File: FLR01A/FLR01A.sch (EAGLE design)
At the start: 10 parts, among them J1 M10SMD_MALE, J2 M10SMD_MALE

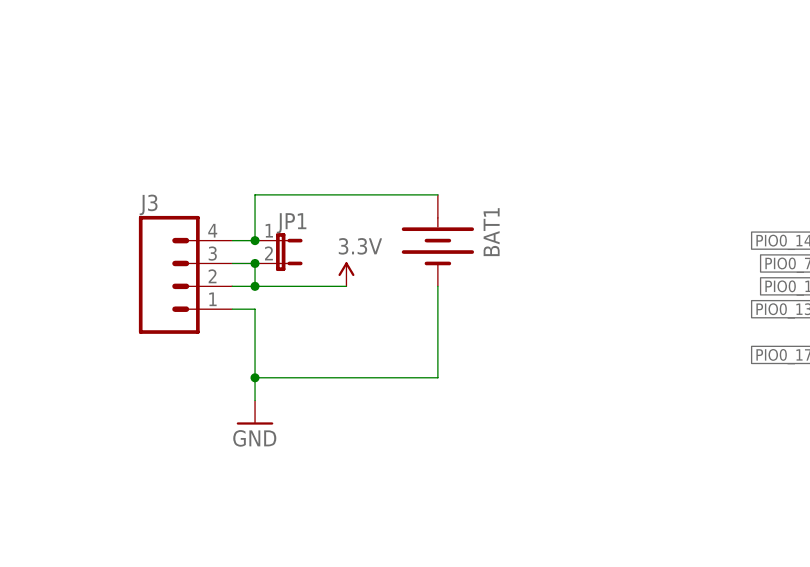
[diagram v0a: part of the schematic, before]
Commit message: [flr] add ptc fuse in series with battery
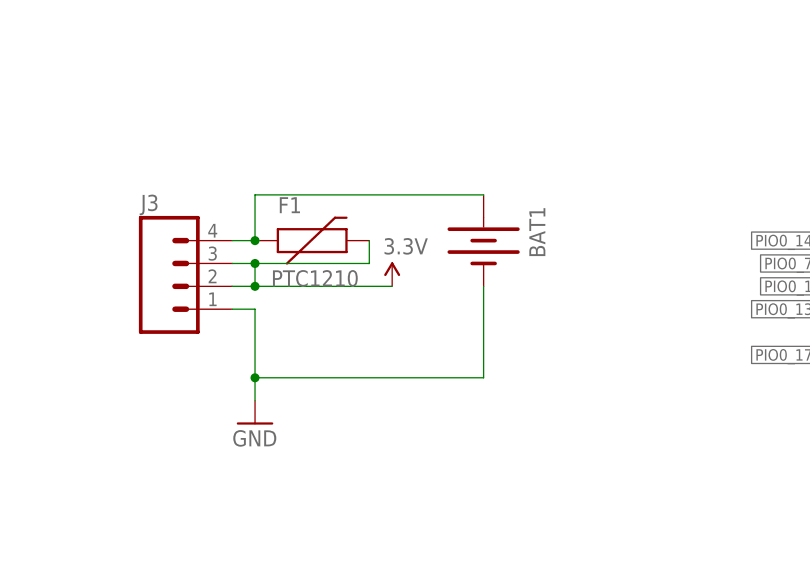
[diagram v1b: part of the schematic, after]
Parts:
- removed JP1: (no value), SparkFun-Passives:JUMPER-2SMD-NC
- added F1: PTC1210, flukso:PTC1210
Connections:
- net 3.3V: now also F1.2; no longer JP1.2
- net N$1: now also F1.1; no longer JP1.1
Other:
- moved on the sheet: BAT1
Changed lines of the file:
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@@
 <part name="BAT1" library="SparkFun-Electromechanical" deviceset="BATTERY" device="245PTH"/>
 <part name="GND1" library="sparkFun" deviceset="GND" device=""/>
-<part name="JP1" library="SparkFun-Passives" deviceset="JUMPER-2" device="SMD-NC"/>
 <part name="P+1" library="sparkFun" deviceset="3.3V" device=""/>
 <part name="J3" library="SparkFun-Connectors" deviceset="M04" device="1X04_NO_SILK"/>
@@
 <part name="S1" library="SparkFun-Electromechanical" deviceset="SWITCH-MOMENTARY-2" device="SMD"/>
 <part name="GND2" library="sparkFun" deviceset="GND" device=""/>
+<part name="F1" library="flukso" deviceset="PTC" device="1210"/>
 </parts>
 <sheets>
@@
 <instance part="FRAME1" gate="G$2" x="162.56" y="0"/>
 <instance part="U$1" gate="G$1" x="15.24" y="12.7"/>
-<instance part="P+2" gate="G$1" x="99.06" y="96.52"/>
+<instance part="P+2" gate="G$1" x="104.14" y="96.52"/>
 <instance part="GND8" gate="1" x="165.1" y="78.74"/>
 <instance part="C1" gate="G$1" x="187.96" y="104.14"/>
@@
 <attribute name="NAME" x="55.88" y="171.45" size="1.778" layer="95"/>
 </instance>
-<instance part="BAT1" gate="G$1" x="109.22" y="101.6" rot="R270"/>
+<instance part="BAT1" gate="G$1" x="114.3" y="101.6" rot="R270"/>
 <instance part="GND1" gate="1" x="88.9" y="81.28"/>
-<instance part="JP1" gate="A" x="91.44" y="101.6" rot="R270"/>
 <instance part="P+1" gate="G$1" x="167.64" y="111.76"/>
 <instance part="J3" gate="G$1" x="81.28" y="96.52"/>
@@
 </instance>
 <instance part="GND2" gate="1" x="40.64" y="139.7"/>
+<instance part="F1" gate="G$1" x="93.98" y="101.6"/>
 </instances>
 <busses>
@@
 <pinref part="BAT1" gate="G$1" pin="-"/>
 <wire x1="88.9" y1="86.36" x2="88.9" y2="83.82" width="0.1524" layer="91"/>
-<wire x1="109.22" y1="96.52" x2="109.22" y2="86.36" width="0.1524" layer="91"/>
-<wire x1="109.22" y1="86.36" x2="88.9" y2="86.36" width="0.1524" layer="91"/>
+<wire x1="114.3" y1="96.52" x2="114.3" y2="86.36" width="0.1524" layer="91"/>
+<wire x1="114.3" y1="86.36" x2="88.9" y2="86.36" width="0.1524" layer="91"/>
 <junction x="88.9" y="86.36"/>
 <pinref part="J3" gate="G$1" pin="1"/>
@@
 </segment>
 <segment>
-<pinref part="JP1" gate="A" pin="2"/>
 <pinref part="J3" gate="G$1" pin="3"/>
 <wire x1="88.9" y1="99.06" x2="86.36" y2="99.06" width="0.1524" layer="91"/>
@@
 <wire x1="88.9" y1="99.06" x2="88.9" y2="96.52" width="0.1524" layer="91"/>
 <wire x1="88.9" y1="96.52" x2="86.36" y2="96.52" width="0.1524" layer="91"/>
+<pinref part="P+2" gate="G$1" pin="3.3V"/>
+<wire x1="88.9" y1="96.52" x2="104.14" y2="96.52" width="0.1524" layer="91"/>
+<junction x="88.9" y="96.52"/>
+<pinref part="F1" gate="G$1" pin="2"/>
+<wire x1="101.6" y1="101.6" x2="101.6" y2="99.06" width="0.1524" layer="91"/>
+<wire x1="101.6" y1="99.06" x2="88.9" y2="99.06" width="0.1524" layer="91"/>
 <junction x="88.9" y="99.06"/>
-<pinref part="P+2" gate="G$1" pin="3.3V"/>
-<wire x1="88.9" y1="96.52" x2="99.06" y2="96.52" width="0.1524" layer="91"/>
-<junction x="88.9" y="96.52"/>
 </segment>
 </net>
@@
 <segment>
 <pinref part="BAT1" gate="G$1" pin="+"/>
-<wire x1="109.22" y1="106.68" x2="88.9" y2="106.68" width="0.1524" layer="91"/>
+<wire x1="114.3" y1="106.68" x2="88.9" y2="106.68" width="0.1524" layer="91"/>
 <wire x1="88.9" y1="106.68" x2="88.9" y2="101.6" width="0.1524" layer="91"/>
 <pinref part="J3" gate="G$1" pin="4"/>
 <wire x1="88.9" y1="101.6" x2="86.36" y2="101.6" width="0.1524" layer="91"/>
-<pinref part="JP1" gate="A" pin="1"/>
+<pinref part="F1" gate="G$1" pin="1"/>
 <junction x="88.9" y="101.6"/>
 </segment>

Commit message: [flk/flr] introduce r3 of sensor and radio board
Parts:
- J1, J2: value M10SMD_MALE -> M10SMD_MALE_SHORT; device flukso:M10SMD_MALE -> flukso:M10SMD_MALE_SHORT
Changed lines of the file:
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@@
 <part name="U$5" library="flukso" deviceset="RFM12B" device=""/>
 <part name="GND25" library="sparkFun" deviceset="GND" device=""/>
-<part name="J1" library="flukso" deviceset="M10" device="SMD_MALE"/>
-<part name="J2" library="flukso" deviceset="M10" device="SMD_MALE"/>
 <part name="BAT1" library="SparkFun-Electromechanical" deviceset="BATTERY" device="245PTH"/>
 <part name="GND1" library="sparkFun" deviceset="GND" device=""/>
@@
 <part name="GND2" library="sparkFun" deviceset="GND" device=""/>
 <part name="F1" library="flukso" deviceset="PTC" device="1210"/>
+<part name="J1" library="flukso" deviceset="M10" device="SMD_MALE_SHORT"/>
+<part name="J2" library="flukso" deviceset="M10" device="SMD_MALE_SHORT"/>
 </parts>
 <sheets>
@@
 <instance part="U$5" gate="G$1" x="167.64" y="96.52"/>
 <instance part="GND25" gate="1" x="170.18" y="78.74"/>
-<instance part="J1" gate="G$1" x="10.16" y="162.56" smashed="yes">
-<attribute name="NAME" x="10.16" y="171.45" size="1.778" layer="95"/>
-</instance>
-<instance part="J2" gate="G$1" x="55.88" y="162.56" smashed="yes">
-<attribute name="NAME" x="55.88" y="171.45" size="1.778" layer="95"/>
-</instance>
 <instance part="BAT1" gate="G$1" x="114.3" y="101.6" rot="R270"/>
 <instance part="GND1" gate="1" x="88.9" y="81.28"/>
@@
 <instance part="GND2" gate="1" x="40.64" y="139.7"/>
 <instance part="F1" gate="G$1" x="93.98" y="101.6"/>
+<instance part="J1" gate="G$1" x="10.16" y="162.56" smashed="yes">
+<attribute name="NAME" x="10.16" y="171.45" size="1.778" layer="95"/>
+</instance>
+<instance part="J2" gate="G$1" x="55.88" y="162.56" smashed="yes">
+<attribute name="NAME" x="55.88" y="171.45" size="1.778" layer="95"/>
+</instance>
 </instances>
 <busses>
@@
 </segment>
 <segment>
-<pinref part="J2" gate="G$1" pin="6"/>
 <wire x1="66.04" y1="157.48" x2="68.58" y2="157.48" width="0.1524" layer="91"/>
 <label x="68.58" y="157.48" size="1.27" layer="95" xref="yes"/>
+<pinref part="J2" gate="G$1" pin="6"/>
 </segment>
 <segment>
@@
 <net name="3.3V" class="0">
 <segment>
-<pinref part="J2" gate="G$1" pin="5"/>
 <wire x1="66.04" y1="154.94" x2="68.58" y2="154.94" width="0.1524" layer="91"/>
 <label x="68.58" y="154.94" size="1.27" layer="95" xref="yes"/>
+<pinref part="J2" gate="G$1" pin="5"/>
 </segment>
 <segment>
@@
 <net name="PIO0_16" class="0">
 <segment>
-<pinref part="J1" gate="G$1" pin="10"/>
 <wire x1="20.32" y1="167.64" x2="22.86" y2="167.64" width="0.1524" layer="91"/>
 <label x="22.86" y="167.64" size="1.27" layer="95" xref="yes"/>
+<pinref part="J1" gate="G$1" pin="10"/>
 </segment>
 </net>
 <net name="I2C0_SCL" class="0">
 <segment>
-<pinref part="J1" gate="G$1" pin="9"/>
 <wire x1="20.32" y1="165.1" x2="22.86" y2="165.1" width="0.1524" layer="91"/>
 <label x="22.86" y="165.1" size="1.27" layer="95" xref="yes"/>
+<pinref part="J1" gate="G$1" pin="9"/>
 </segment>
 </net>
 <net name="I2C0_SDA" class="0">
 <segment>
-<pinref part="J1" gate="G$1" pin="8"/>
 <wire x1="20.32" y1="162.56" x2="22.86" y2="162.56" width="0.1524" layer="91"/>
 <label x="22.86" y="162.56" size="1.27" layer="95" xref="yes"/>
+<pinref part="J1" gate="G$1" pin="8"/>
 </segment>
 </net>
 <net name="PIO0_2" class="0">
 <segment>
-<pinref part="J1" gate="G$1" pin="7"/>
 <wire x1="20.32" y1="160.02" x2="22.86" y2="160.02" width="0.1524" layer="91"/>
 <label x="22.86" y="160.02" size="1.27" layer="95" xref="yes"/>
+<pinref part="J1" gate="G$1" pin="7"/>
 </segment>
 </net>
 <net name="PIO0_3" class="0">
 <segment>
-<pinref part="J1" gate="G$1" pin="6"/>
 <wire x1="20.32" y1="157.48" x2="22.86" y2="157.48" width="0.1524" layer="91"/>
 <label x="22.86" y="157.48" size="1.27" layer="95" xref="yes"/>
+<pinref part="J1" gate="G$1" pin="6"/>
 </segment>
 </net>
 <net name="PIO0_4" class="0">
 <segment>
-<pinref part="J1" gate="G$1" pin="5"/>
 <wire x1="20.32" y1="154.94" x2="22.86" y2="154.94" width="0.1524" layer="91"/>
 <label x="22.86" y="154.94" size="1.27" layer="95" xref="yes"/>
+<pinref part="J1" gate="G$1" pin="5"/>
 </segment>
 </net>
 <net name="PIO0_5" class="0">
 <segment>
-<pinref part="J1" gate="G$1" pin="4"/>
 <wire x1="20.32" y1="152.4" x2="40.64" y2="152.4" width="0.1524" layer="91"/>
 <label x="43.18" y="152.4" size="1.27" layer="95" xref="yes"/>
@@
 <wire x1="40.64" y1="152.4" x2="43.18" y2="152.4" width="0.1524" layer="91"/>
 <junction x="40.64" y="152.4"/>
+<pinref part="J1" gate="G$1" pin="4"/>
 </segment>
 </net>
 <net name="PIO0_12" class="0">
 <segment>
-<pinref part="J1" gate="G$1" pin="3"/>
 <wire x1="20.32" y1="149.86" x2="22.86" y2="149.86" width="0.1524" layer="91"/>
 <label x="22.86" y="149.86" size="1.27" layer="95" xref="yes"/>
+<pinref part="J1" gate="G$1" pin="3"/>
 </segment>
 </net>
 <net name="PIO0_13" class="0">
 <segment>
-<pinref part="J1" gate="G$1" pin="2"/>
 <wire x1="20.32" y1="147.32" x2="22.86" y2="147.32" width="0.1524" layer="91"/>
 <label x="22.86" y="147.32" size="1.27" layer="95" xref="yes"/>
+<pinref part="J1" gate="G$1" pin="2"/>
 </segment>
 <segment>
@@
 <net name="PIO0_17" class="0">
 <segment>
-<pinref part="J1" gate="G$1" pin="1"/>
 <wire x1="20.32" y1="144.78" x2="22.86" y2="144.78" width="0.1524" layer="91"/>
 <label x="22.86" y="144.78" size="1.27" layer="95" xref="yes"/>
+<pinref part="J1" gate="G$1" pin="1"/>
 </segment>
 <segment>
@@
 <net name="PIO0_14" class="0">
 <segment>
-<pinref part="J2" gate="G$1" pin="10"/>
 <wire x1="66.04" y1="167.64" x2="68.58" y2="167.64" width="0.1524" layer="91"/>
 <label x="68.58" y="167.64" size="1.27" layer="95" xref="yes"/>
+<pinref part="J2" gate="G$1" pin="10"/>
 </segment>
 <segment>
@@
 <net name="PIO0_0" class="0">
 <segment>
-<pinref part="J2" gate="G$1" pin="9"/>
 <wire x1="66.04" y1="165.1" x2="68.58" y2="165.1" width="0.1524" layer="91"/>
 <label x="68.58" y="165.1" size="1.27" layer="95" xref="yes"/>
+<pinref part="J2" gate="G$1" pin="9"/>
 </segment>
 </net>
 <net name="PIO0_6" class="0">
 <segment>
-<pinref part="J2" gate="G$1" pin="8"/>
 <wire x1="66.04" y1="162.56" x2="68.58" y2="162.56" width="0.1524" layer="91"/>
 <label x="68.58" y="162.56" size="1.27" layer="95" xref="yes"/>
+<pinref part="J2" gate="G$1" pin="8"/>
 </segment>
 </net>
 <net name="PIO0_7" class="0">
 <segment>
-<pinref part="J2" gate="G$1" pin="7"/>
 <wire x1="66.04" y1="160.02" x2="68.58" y2="160.02" width="0.1524" layer="91"/>
 <label x="68.58" y="160.02" size="1.27" layer="95" xref="yes"/>
+<pinref part="J2" gate="G$1" pin="7"/>
 </segment>
 <segment>
@@
 <net name="PIO0_8" class="0">
 <segment>
-<pinref part="J2" gate="G$1" pin="4"/>
 <wire x1="66.04" y1="152.4" x2="68.58" y2="152.4" width="0.1524" layer="91"/>
 <label x="68.58" y="152.4" size="1.27" layer="95" xref="yes"/>
+<pinref part="J2" gate="G$1" pin="4"/>
 </segment>
 </net>
 <net name="PIO0_9" class="0">
 <segment>
-<pinref part="J2" gate="G$1" pin="3"/>
 <wire x1="66.04" y1="149.86" x2="68.58" y2="149.86" width="0.1524" layer="91"/>
 <label x="68.58" y="149.86" size="1.27" layer="95" xref="yes"/>
+<pinref part="J2" gate="G$1" pin="3"/>
 </segment>
 </net>
 <net name="PIO0_1" class="0">
 <segment>
-<pinref part="J2" gate="G$1" pin="2"/>
 <wire x1="66.04" y1="147.32" x2="68.58" y2="147.32" width="0.1524" layer="91"/>
 <label x="68.58" y="147.32" size="1.27" layer="95" xref="yes"/>
+<pinref part="J2" gate="G$1" pin="2"/>
 </segment>
 <segment>
@@
 <net name="PIO0_15" class="0">
 <segment>
-<pinref part="J2" gate="G$1" pin="1"/>
 <wire x1="66.04" y1="144.78" x2="68.58" y2="144.78" width="0.1524" layer="91"/>
 <label x="68.58" y="144.78" size="1.27" layer="95" xref="yes"/>
-</segment>
-</net>
+<pinref part="J2" gate="G$1" pin="1"/>
+</segment>
+</net>

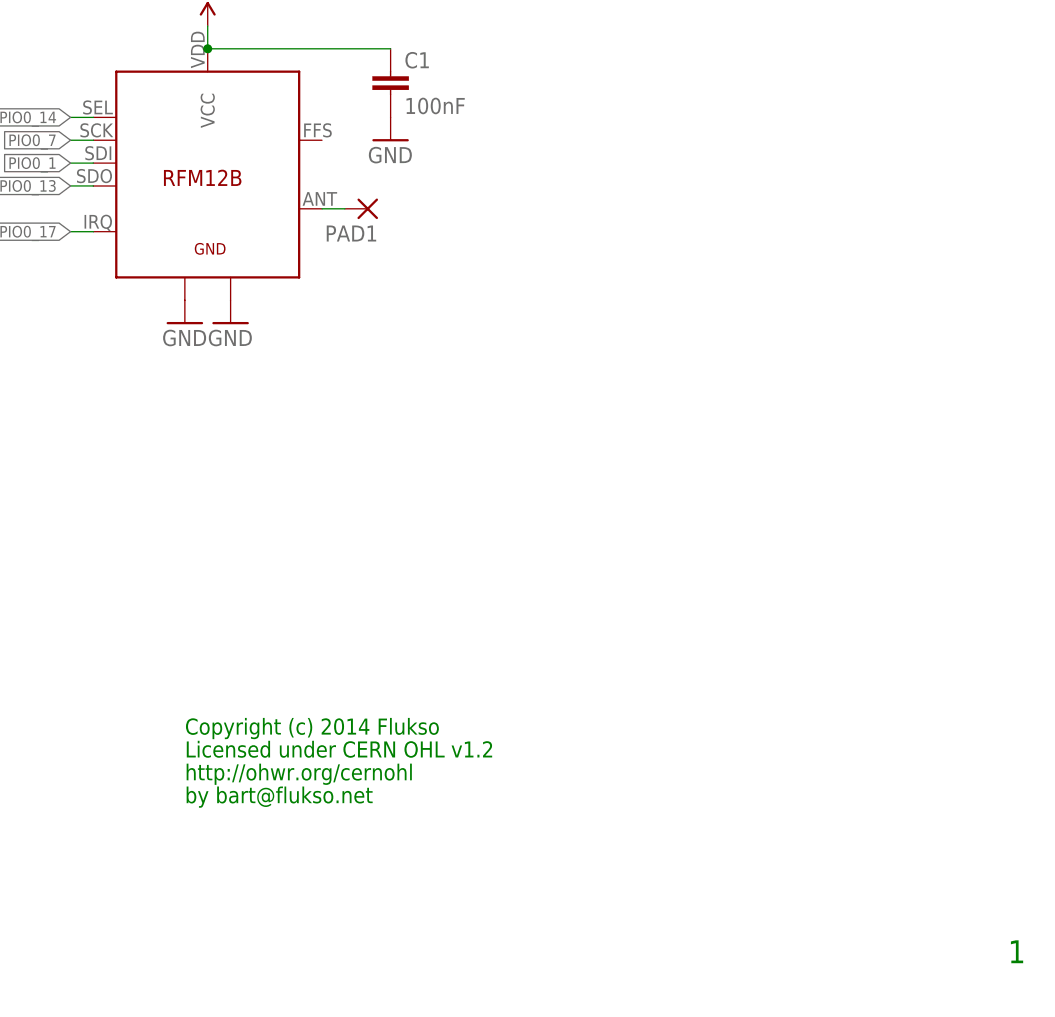
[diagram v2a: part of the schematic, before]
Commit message: [flk/flr] adapt board layout to new M10 footprints + power switch
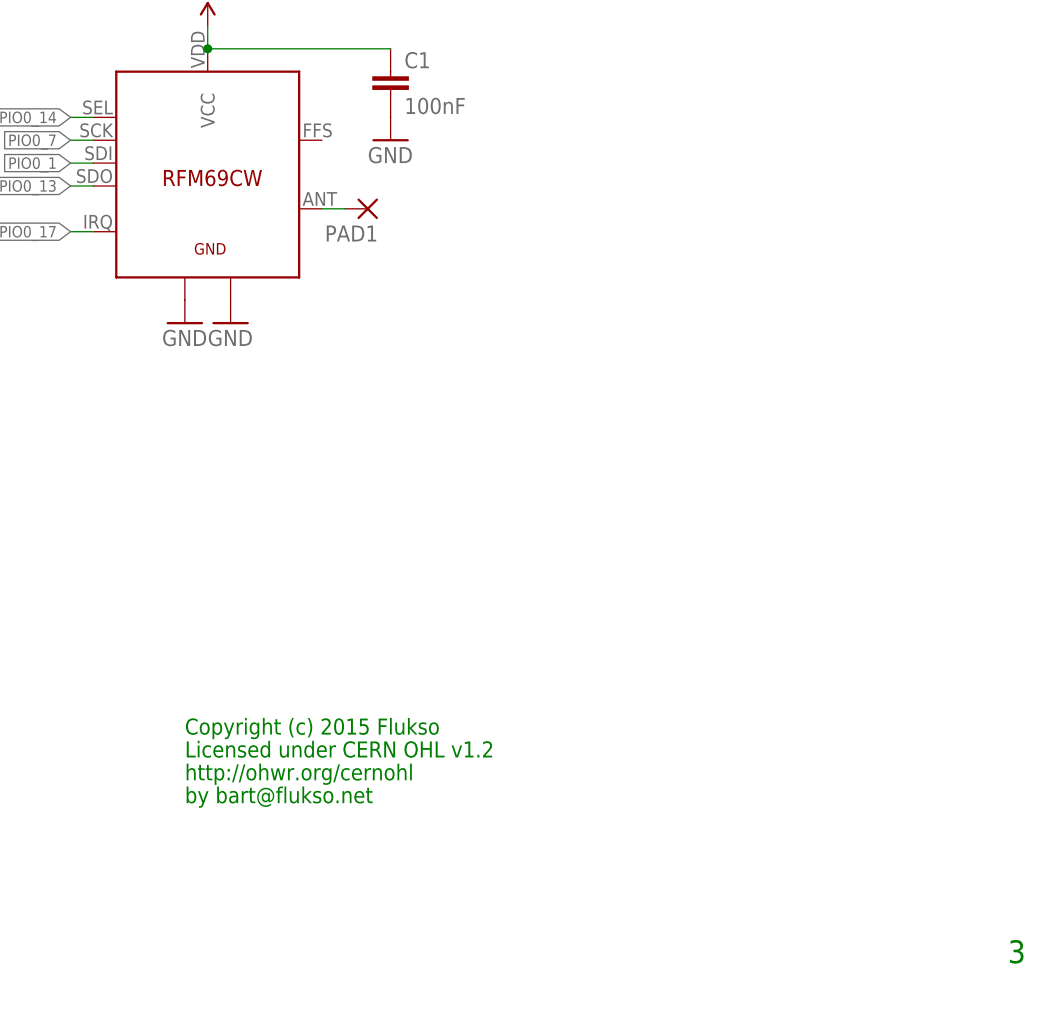
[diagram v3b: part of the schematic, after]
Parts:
- removed U$5: RFM12B, flukso:RFM12B
- added U$2: RFM69CW, flukso:RFM69CW
- J1, J2: value M10SMD_MALE_SHORT -> M10SMD_FEMALE_SHORT; device flukso:M10SMD_MALE_SHORT -> flukso:M10SMD_FEMALE_SHORT
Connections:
- net 3.3V: now also U$2.VCC; no longer U$5.VCC
- net GND: now also U$2.GND1, U$2.GND2; no longer U$5.GND1, U$5.GND2
- net N$6: now also U$2.ANT; no longer U$5.ANT
- net PIO0_1: now also U$2.SDI; no longer U$5.SDI
- net PIO0_13: now also U$2.SDO; no longer U$5.SDO
- net PIO0_14: now also U$2.SEL; no longer U$5.SEL
- net PIO0_17: now also U$2.IRQ; no longer U$5.IRQ
- net PIO0_7: now also U$2.SCK; no longer U$5.SCK
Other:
- note added: "3"
- note added: "Copyright (c) 2015 Flukso"
- note removed: "1"
- note removed: "Copyright (c) 2014 Flukso"
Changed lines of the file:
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@@
 <part name="C1" library="sparkFun" deviceset="CAP" device="0402-CAP" value="100nF"/>
 <part name="GND12" library="sparkFun" deviceset="GND" device=""/>
-<part name="U$5" library="flukso" deviceset="RFM12B" device=""/>
 <part name="GND25" library="sparkFun" deviceset="GND" device=""/>
 <part name="BAT1" library="SparkFun-Electromechanical" deviceset="BATTERY" device="245PTH"/>
@@
 <part name="GND2" library="sparkFun" deviceset="GND" device=""/>
 <part name="F1" library="flukso" deviceset="PTC" device="1210"/>
-<part name="J1" library="flukso" deviceset="M10" device="SMD_MALE_SHORT"/>
-<part name="J2" library="flukso" deviceset="M10" device="SMD_MALE_SHORT"/>
+<part name="J1" library="flukso" deviceset="M10" device="SMD_FEMALE_SHORT"/>
+<part name="J2" library="flukso" deviceset="M10" device="SMD_FEMALE_SHORT"/>
+<part name="U$2" library="flukso" deviceset="RFM69CW" device=""/>
 </parts>
 <sheets>
 <sheet>
 <plain>
-<text x="256.54" y="7.62" size="2.54" layer="91">1</text>
-<text x="165.1" y="33.02" size="1.778" layer="91">Copyright (c) 2014 Flukso</text>
+<text x="256.54" y="7.62" size="2.54" layer="91">3</text>
+<text x="165.1" y="33.02" size="1.778" layer="91">Copyright (c) 2015 Flukso</text>
 <text x="165.1" y="30.48" size="1.778" layer="91">Licensed under CERN OHL v1.2</text>
 <text x="165.1" y="27.94" size="1.778" layer="91">http://ohwr.org/cernohl</text>
@@
 <instance part="C1" gate="G$1" x="187.96" y="104.14"/>
 <instance part="GND12" gate="1" x="187.96" y="99.06"/>
-<instance part="U$5" gate="G$1" x="167.64" y="96.52"/>
 <instance part="GND25" gate="1" x="170.18" y="78.74"/>
 <instance part="BAT1" gate="G$1" x="114.3" y="101.6" rot="R270"/>
@@
 <attribute name="NAME" x="55.88" y="171.45" size="1.778" layer="95"/>
 </instance>
+<instance part="U$2" gate="G$1" x="167.64" y="96.52"/>
 </instances>
 <busses>
@@
 <pinref part="GND8" gate="1" pin="GND"/>
 <pinref part="GND25" gate="1" pin="GND"/>
-<pinref part="U$5" gate="G$1" pin="GND2"/>
-<pinref part="U$5" gate="G$1" pin="GND1"/>
+<pinref part="U$2" gate="G$1" pin="GND2"/>
+<pinref part="U$2" gate="G$1" pin="GND1"/>
 </segment>
 <segment>
@@
 </segment>
 <segment>
-<pinref part="U$5" gate="G$1" pin="VCC"/>
 <pinref part="P+1" gate="G$1" pin="3.3V"/>
 <wire x1="167.64" y1="109.22" x2="167.64" y2="111.76" width="0.1524" layer="91"/>
 <pinref part="C1" gate="G$1" pin="1"/>
 <wire x1="187.96" y1="109.22" x2="167.64" y2="109.22" width="0.1524" layer="91"/>
+<pinref part="U$2" gate="G$1" pin="VCC"/>
 <junction x="167.64" y="109.22"/>
 </segment>
@@
 <segment>
 <wire x1="180.34" y1="91.44" x2="182.88" y2="91.44" width="0.2032" layer="91"/>
-<pinref part="U$5" gate="G$1" pin="ANT"/>
 <pinref part="PAD1" gate="P" pin="P"/>
+<pinref part="U$2" gate="G$1" pin="ANT"/>
 </segment>
 </net>
@@
 </segment>
 <segment>
-<pinref part="U$5" gate="G$1" pin="SDO"/>
 <wire x1="154.94" y1="93.98" x2="152.4" y2="93.98" width="0.1524" layer="91"/>
 <label x="152.4" y="93.98" size="1.27" layer="95" rot="R180" xref="yes"/>
+<pinref part="U$2" gate="G$1" pin="SDO"/>
 </segment>
 </net>
@@
 </segment>
 <segment>
-<pinref part="U$5" gate="G$1" pin="IRQ"/>
 <wire x1="154.94" y1="88.9" x2="152.4" y2="88.9" width="0.1524" layer="91"/>
 <label x="152.4" y="88.9" size="1.27" layer="95" rot="R180" xref="yes"/>
+<pinref part="U$2" gate="G$1" pin="IRQ"/>
 </segment>
 </net>
@@
 <wire x1="154.94" y1="101.6" x2="152.4" y2="101.6" width="0.2032" layer="91"/>
 <label x="152.4" y="101.6" size="1.27" layer="95" rot="R180" xref="yes"/>
-<pinref part="U$5" gate="G$1" pin="SEL"/>
+<pinref part="U$2" gate="G$1" pin="SEL"/>
 </segment>
 </net>
@@
 </segment>
 <segment>
-<pinref part="U$5" gate="G$1" pin="SCK"/>
 <wire x1="154.94" y1="99.06" x2="152.4" y2="99.06" width="0.1524" layer="91"/>
 <label x="152.4" y="99.06" size="1.27" layer="95" rot="R180" xref="yes"/>
+<pinref part="U$2" gate="G$1" pin="SCK"/>
 </segment>
 </net>
@@
 </segment>
 <segment>
-<pinref part="U$5" gate="G$1" pin="SDI"/>
 <wire x1="154.94" y1="96.52" x2="152.4" y2="96.52" width="0.1524" layer="91"/>
 <label x="152.4" y="96.52" size="1.27" layer="95" rot="R180" xref="yes"/>
-</segment>
-</net>
+<pinref part="U$2" gate="G$1" pin="SDI"/>
+</segment>
+</net>
